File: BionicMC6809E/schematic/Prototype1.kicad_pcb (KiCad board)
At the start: 2 copper layers, 48.3 x 71.1 mm, 9 parts, among them J1 BionicConnector, U1 MC6809P, U2 74HCT126

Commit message: [BionicMC6809E] Mezzanine board
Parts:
- U1: value MC6809P -> MC6809EP
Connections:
- U1 pad 33: /P54 -> /P44
- U1 pad 34: /P47 -> Net-(U1-Pad34)
- U1 pad 35: /P44 -> /P47
- U1 pad 36: /P52 -> /P50
- U1 pad 38: /P46 -> /P52
- U1 pad 39: GND -> /P54
- U2 pad 4: GND -> VCC
- U2 pad 5: GND -> /P46
- U2 pad 6: Net-(U2-Pad6) -> Net-(U1-Pad34)
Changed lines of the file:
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@@
     (zones 0)
     (modules 9)
-    (nets 60)
+    (nets 61)
   )
   (page A4)
@@
   (net 45 /P45)
   (net 46 /#RESET)
-  (net 47 "Net-(U2-Pad6)")
-  (net 48 "Net-(U2-Pad11)")
-  (net 49 "Net-(U2-Pad8)")
-  (net 50 /P33)
-  (net 51 /P32)
-  (net 52 /P31)
-  (net 53 /P30)
-  (net 54 /P51)
-  (net 55 /P55)
-  (net 56 /P43)
-  (net 57 /P37)
-  (net 58 /P52)
-  (net 59 /P54)
+  (net 47 "Net-(U2-Pad11)")
+  (net 48 "Net-(U2-Pad8)")
+  (net 49 /P33)
+  (net 50 /P32)
+  (net 51 /P31)
+  (net 52 /P30)
+  (net 53 /P51)
+  (net 54 /P55)
+  (net 55 /P43)
+  (net 56 /P37)
+  (net 57 /P52)
+  (net 58 /P54)
+  (net 59 /P50)
+  (net 60 "Net-(U1-Pad34)")
   (net_class Default "This is the default net class."
     (clearance 0.2)
@@
     (add_net /P46)
     (add_net /P47)
+    (add_net /P50)
     (add_net /P51)
     (add_net /P52)
@@
     (add_net "Net-(J1-Pad46)")
     (add_net "Net-(J1-Pad47)")
+    (add_net "Net-(U1-Pad34)")
     (add_net "Net-(U2-Pad11)")
-    (add_net "Net-(U2-Pad6)")
     (add_net "Net-(U2-Pad8)")
     (add_net VCC)
@@
       (effects (font (size 1 1) (thickness 0.15)))
     )
-    (fp_text value MC6809P (at 7.62 50.59) (layer F.Fab)
+    (fp_text value MC6809EP (at 7.62 50.59) (layer F.Fab)
       (effects (font (size 1 1) (thickness 0.15)))
     )
@@
       (net 28 /P34))
     (pad 39 thru_hole oval (at 15.24 2.54) (size 1.6 1.6) (drill 0.8) (layers *.Cu *.Mask)
-      (net 2 GND))
+      (net 58 /P54))
     (pad 19 thru_hole oval (at 0 45.72) (size 1.6 1.6) (drill 0.8) (layers *.Cu *.Mask)
-      (net 50 /P33))
+      (net 49 /P33))
     (pad 38 thru_hole oval (at 15.24 5.08) (size 1.6 1.6) (drill 0.8) (layers *.Cu *.Mask)
-      (net 14 /P46))
+      (net 57 /P52))
     (pad 18 thru_hole oval (at 0 43.18) (size 1.6 1.6) (drill 0.8) (layers *.Cu *.Mask)
-      (net 51 /P32))
+      (net 50 /P32))
     (pad 37 thru_hole oval (at 15.24 7.62) (size 1.6 1.6) (drill 0.8) (layers *.Cu *.Mask)
       (net 46 /#RESET))
     (pad 17 thru_hole oval (at 0 40.64) (size 1.6 1.6) (drill 0.8) (layers *.Cu *.Mask)
-      (net 52 /P31))
+      (net 51 /P31))
     (pad 36 thru_hole oval (at 15.24 10.16) (size 1.6 1.6) (drill 0.8) (layers *.Cu *.Mask)
-      (net 58 /P52))
+      (net 59 /P50))
     (pad 16 thru_hole oval (at 0 38.1) (size 1.6 1.6) (drill 0.8) (layers *.Cu *.Mask)
-      (net 53 /P30))
+      (net 52 /P30))
     (pad 35 thru_hole oval (at 15.24 12.7) (size 1.6 1.6) (drill 0.8) (layers *.Cu *.Mask)
-      (net 43 /P44))
+      (net 11 /P47))
     (pad 15 thru_hole oval (at 0 35.56) (size 1.6 1.6) (drill 0.8) (layers *.Cu *.Mask)
       (net 10 /P27))
     (pad 34 thru_hole oval (at 15.24 15.24) (size 1.6 1.6) (drill 0.8) (layers *.Cu *.Mask)
-      (net 11 /P47))
+      (net 60 "Net-(U1-Pad34)"))
     (pad 14 thru_hole oval (at 0 33.02) (size 1.6 1.6) (drill 0.8) (layers *.Cu *.Mask)
       (net 7 /P26))
     (pad 33 thru_hole oval (at 15.24 17.78) (size 1.6 1.6) (drill 0.8) (layers *.Cu *.Mask)
-      (net 59 /P54))
+      (net 43 /P44))
     (pad 13 thru_hole oval (at 0 30.48) (size 1.6 1.6) (drill 0.8) (layers *.Cu *.Mask)
       (net 17 /P25))
@@
       (net 35 /P15))
     (pad 6 thru_hole oval (at 0 12.7) (size 1.6 1.6) (drill 0.8) (layers *.Cu *.Mask)
-      (net 55 /P55))
+      (net 54 /P55))
     (pad 25 thru_hole oval (at 15.24 38.1) (size 1.6 1.6) (drill 0.8) (layers *.Cu *.Mask)
       (net 33 /P16))
     (pad 5 thru_hole oval (at 0 10.16) (size 1.6 1.6) (drill 0.8) (layers *.Cu *.Mask)
-      (net 54 /P51))
+      (net 53 /P51))
     (pad 24 thru_hole oval (at 15.24 40.64) (size 1.6 1.6) (drill 0.8) (layers *.Cu *.Mask)
       (net 31 /P17))
@@
       (net 45 /P45))
     (pad 23 thru_hole oval (at 15.24 43.18) (size 1.6 1.6) (drill 0.8) (layers *.Cu *.Mask)
-      (net 57 /P37))
+      (net 56 /P37))
     (pad 3 thru_hole oval (at 0 5.08) (size 1.6 1.6) (drill 0.8) (layers *.Cu *.Mask)
       (net 40 /P42))
@@
       (net 32 /P36))
     (pad 2 thru_hole oval (at 0 2.54) (size 1.6 1.6) (drill 0.8) (layers *.Cu *.Mask)
-      (net 56 /P43))
+      (net 55 /P43))
     (pad 21 thru_hole oval (at 15.24 48.26) (size 1.6 1.6) (drill 0.8) (layers *.Cu *.Mask)
       (net 30 /P35))
@@
       (net 2 GND))
     (pad 6 thru_hole oval (at 0 12.7 90) (size 1.6 1.6) (drill 0.8) (layers *.Cu *.Mask)
-      (net 47 "Net-(U2-Pad6)"))
+      (net 60 "Net-(U1-Pad34)"))
     (pad 12 thru_hole oval (at 7.62 5.08 90) (size 1.6 1.6) (drill 0.8) (layers *.Cu *.Mask)
       (net 2 GND))
     (pad 5 thru_hole oval (at 0 10.16 90) (size 1.6 1.6) (drill 0.8) (layers *.Cu *.Mask)
-      (net 2 GND))
+      (net 14 /P46))
     (pad 11 thru_hole oval (at 7.62 7.62 90) (size 1.6 1.6) (drill 0.8) (layers *.Cu *.Mask)
-      (net 48 "Net-(U2-Pad11)"))
+      (net 47 "Net-(U2-Pad11)"))
     (pad 4 thru_hole oval (at 0 7.62 90) (size 1.6 1.6) (drill 0.8) (layers *.Cu *.Mask)
-      (net 2 GND))
+      (net 1 VCC))
     (pad 10 thru_hole oval (at 7.62 10.16 90) (size 1.6 1.6) (drill 0.8) (layers *.Cu *.Mask)
       (net 2 GND))
@@
       (net 4 /P53))
     (pad 8 thru_hole oval (at 7.62 15.24 90) (size 1.6 1.6) (drill 0.8) (layers *.Cu *.Mask)
-      (net 49 "Net-(U2-Pad8)"))
+      (net 48 "Net-(U2-Pad8)"))
     (pad 1 thru_hole rect (at 0 0 90) (size 1.6 1.6) (drill 0.8) (layers *.Cu *.Mask)
       (net 1 VCC))

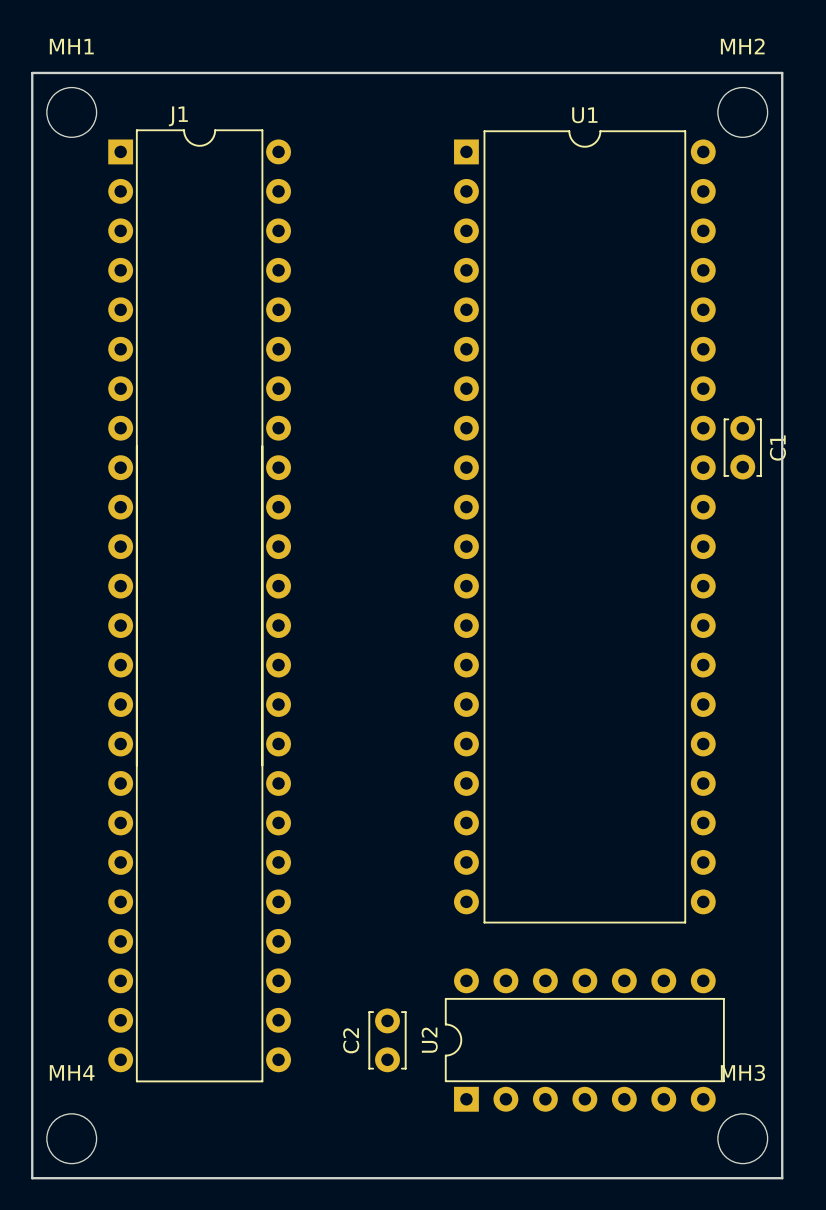
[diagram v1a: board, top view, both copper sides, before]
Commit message: [BionicMC6809E] Tune bus cycle
- Teensy 4.1: Q/E ~ 1.0MHz
- Teensy 3.5: Q/E ~ 230kHz
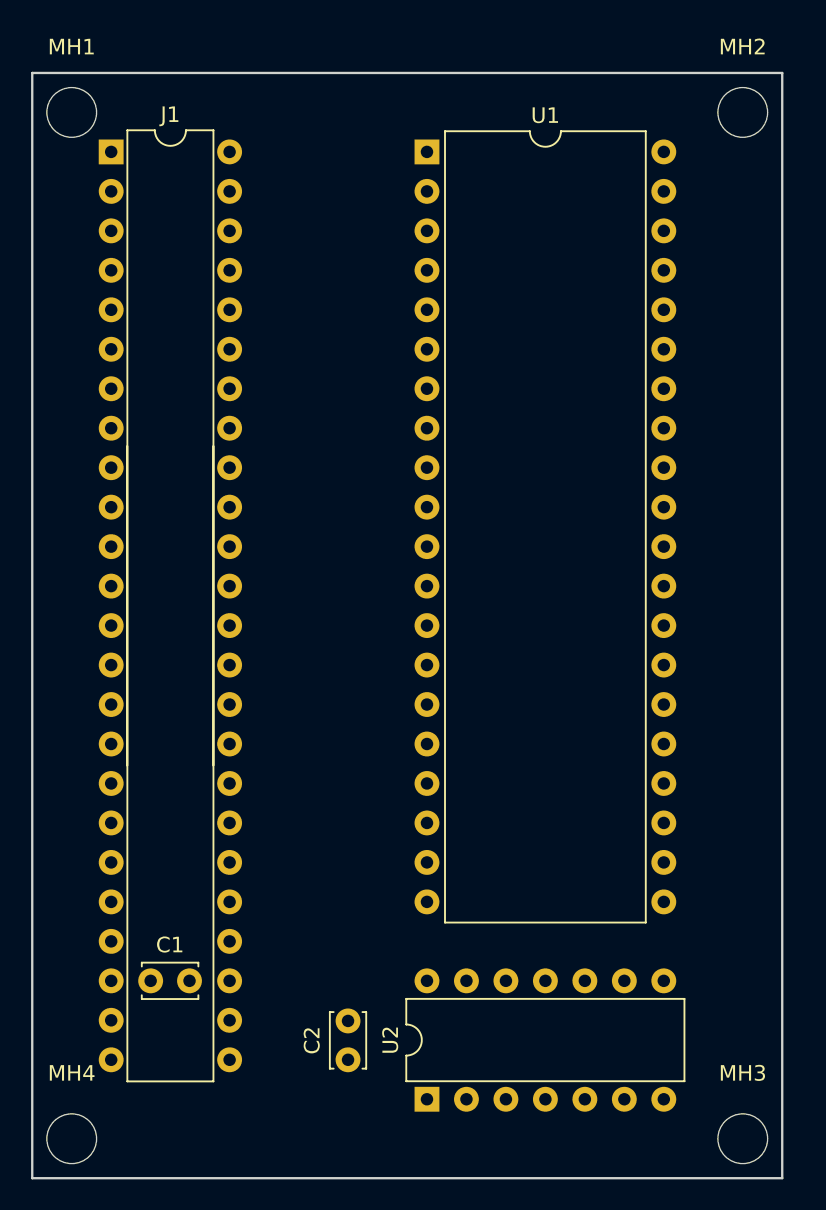
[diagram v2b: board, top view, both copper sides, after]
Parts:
- J1: footprint 0-LocalLibrary:DIP-48_W10.16mm -> 0-LocalLibrary:DIP-48_W7.62mm
- moved C1 52.1 mm to (106.1, 125.9), turned to 0 degrees
- moved U1 2.54 mm to (123.9, 72.5)
- moved U2 2.54 mm to (123.9, 133.5)
- moved C2 2.54 mm to (118.8, 131.0)
- moved J1 0.61 mm to (103.5, 72.5)
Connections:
- J1 pad 20: Net-(J1-Pad20) -> /P50
- J1 pad 21: Net-(J1-Pad21) -> /P51
- J1 pad 22: Net-(J1-Pad22) -> /P52
- J1 pad 28: Net-(J1-Pad28) -> /P55
- J1 pad 29: Net-(J1-Pad29) -> /P54
- J1 pad 35: /P35 -> /P43
- J1 pad 40: /P36 -> /P37
- J1 pad 41: /P35 -> /P36
- J1 pad 42: /P34 -> /P35
- J1 pad 43: Net-(J1-Pad43) -> /P34
- J1 pad 44: Net-(J1-Pad44) -> /P33
- J1 pad 45: Net-(J1-Pad45) -> /P32
- J1 pad 46: Net-(J1-Pad46) -> /P31
- J1 pad 47: Net-(J1-Pad47) -> /P30
- U1 pad 35: /P47 -> Net-(U1-Pad35)
- U2 pad 10: GND -> VCC
- U2 pad 2: /P53 -> /P47
- U2 pad 3: /#RESET -> Net-(U1-Pad35)
- U2 pad 8: Net-(U2-Pad8) -> /#RESET
- U2 pad 9: GND -> /P53

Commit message: Fix Bionic connector pin outs
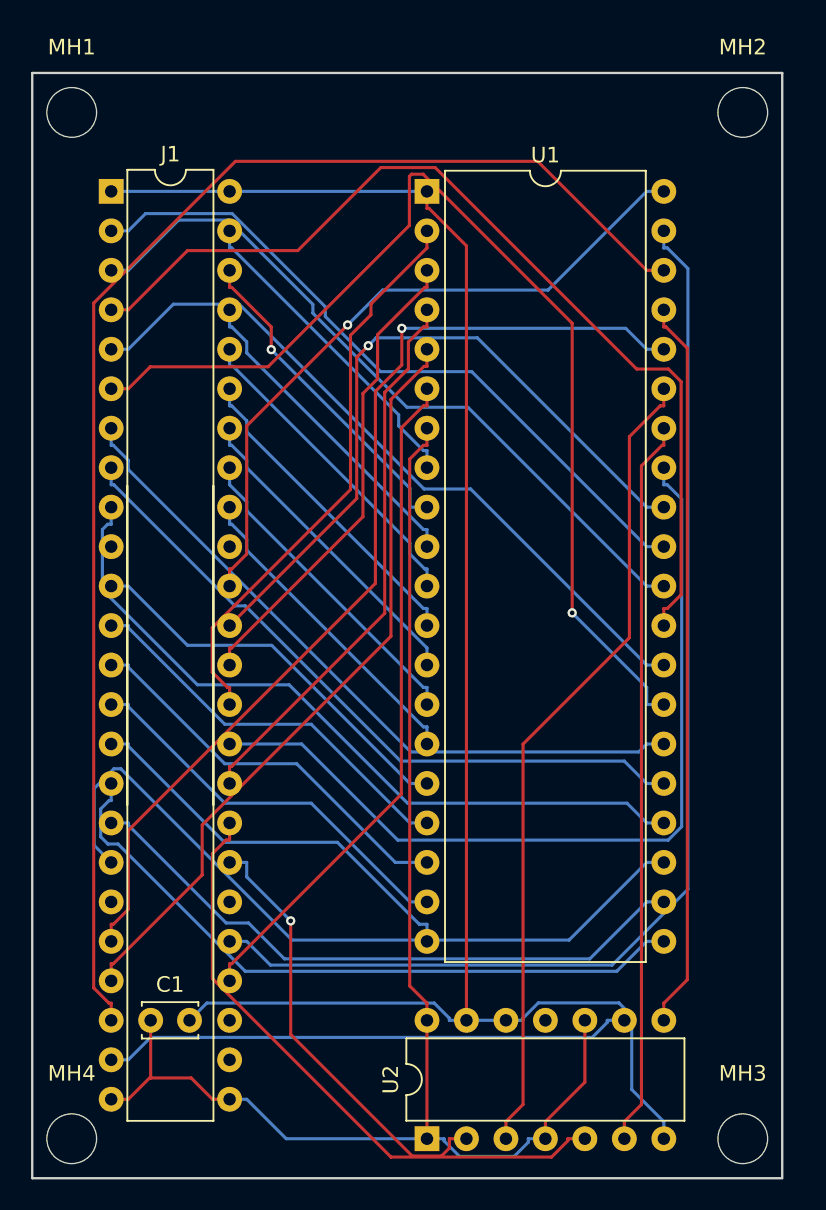
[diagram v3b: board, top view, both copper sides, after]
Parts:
- removed C2: 0.1u, Capacitor_THT:C_Disc_D3.4mm_W2.1mm_P2.50mm
- moved C1 2.54 mm to (106.1, 128.4)
- moved J1 2.54 mm to (103.5, 75.1)
- moved U1 2.54 mm to (123.9, 75.1)
- moved U2 2.54 mm to (123.9, 136.0)
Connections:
- net /#RESET renamed Net-(U1-Pad37)
- J1 pad 11: /P20 -> /P30
- J1 pad 12: /P21 -> /P31
- J1 pad 13: /P22 -> /P32
- J1 pad 14: /P23 -> /P33
- J1 pad 15: /P24 -> /P34
- J1 pad 16: /P25 -> /P35
- J1 pad 17: /P26 -> /P36
- J1 pad 18: /P27 -> /P37
- J1 pad 40: /P37 -> /P27
- J1 pad 41: /P36 -> /P26
- J1 pad 42: /P35 -> /P25
- J1 pad 43: /P34 -> /P24
- J1 pad 44: /P33 -> /P23
- J1 pad 45: /P32 -> /P22
- J1 pad 46: /P31 -> /P21
- J1 pad 47: /P30 -> /P20
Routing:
- net GND: track 0.00 -> 113.9 mm
- net VCC: track 0.00 -> 90.4 mm
- net /P52: track 0.00 -> 90.1 mm
- net /P54: track 0.00 -> 75.3 mm
- net /P14: track 0.00 -> 68.8 mm, vias 0 -> 1
- net /P50: track 0.00 -> 64.7 mm, vias 0 -> 1
- net /P12: track 0.00 -> 62.5 mm
- net /P44: track 0.00 -> 55.7 mm
- net Net-(U1-Pad35): track 0.00 -> 52.6 mm
- net /P51: track 0.00 -> 49.2 mm
- net /P37: track 0.00 -> 49.0 mm
- net /P17: track 0.00 -> 48.0 mm
- net Net-(U1-Pad37): track 0.00 -> 47.1 mm
- net /P11: track 0.00 -> 47.0 mm
- net Net-(U1-Pad34): track 0.00 -> 46.8 mm
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
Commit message: Migrate to KiCad 6.0
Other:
- net class Default removed
